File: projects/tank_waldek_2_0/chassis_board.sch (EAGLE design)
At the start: 22 parts, among them U1 NUCLEO-L432KC

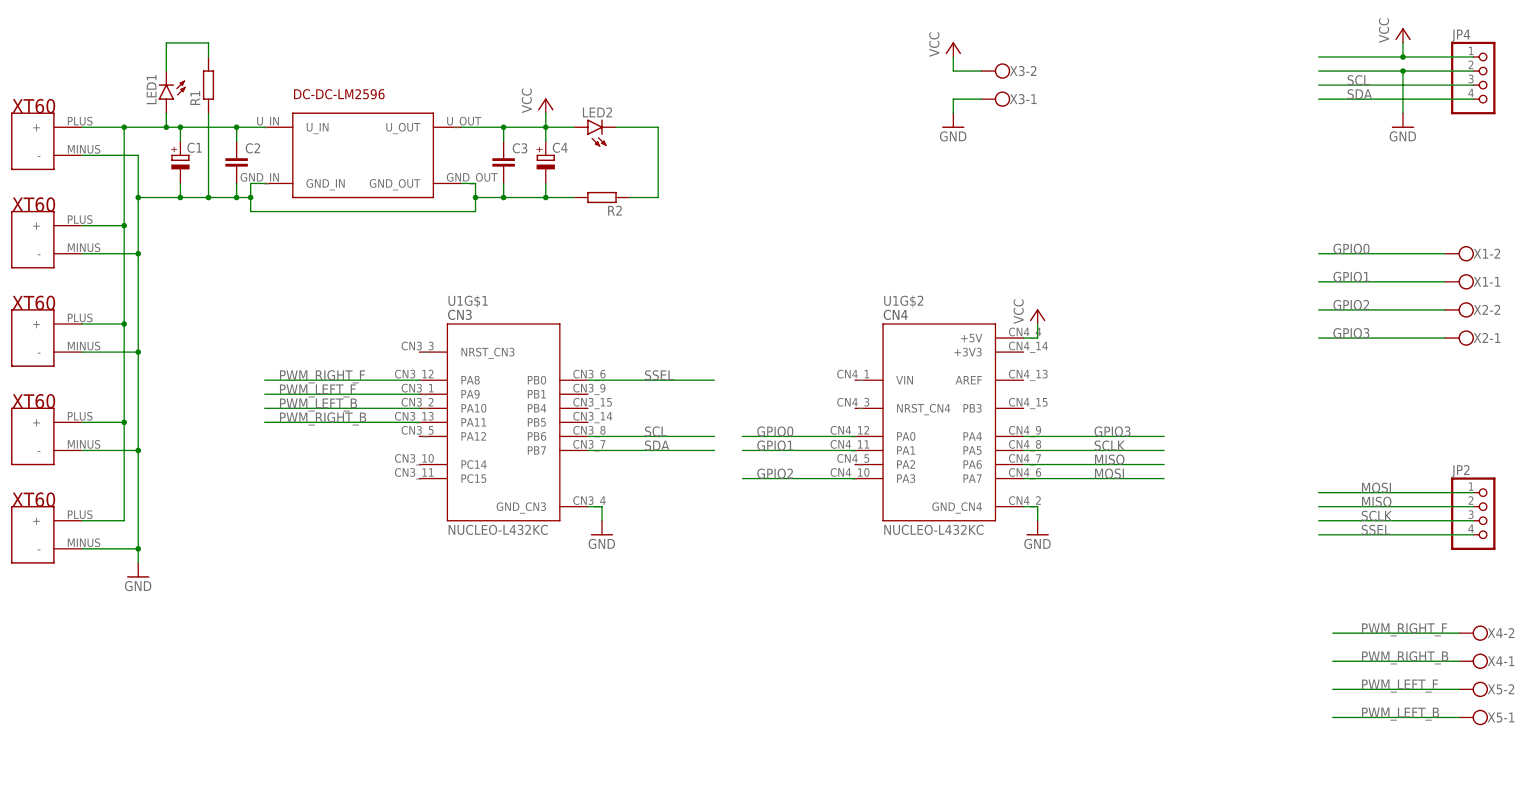
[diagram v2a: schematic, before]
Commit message: updated waldek chassis board and added new rpi shield
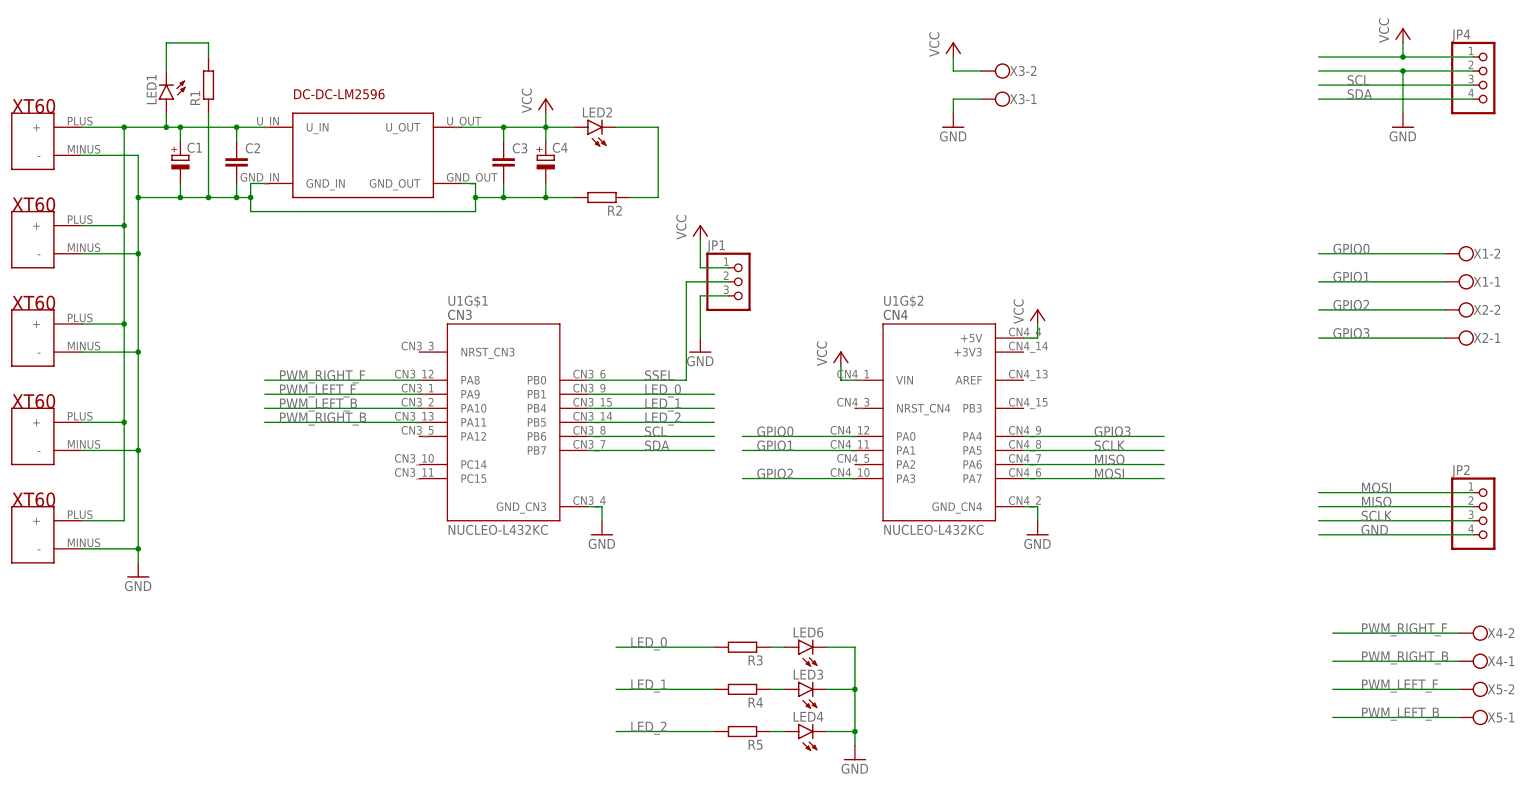
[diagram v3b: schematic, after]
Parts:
- added JP1: (no value), pinhead:PINHD-1X3
- added LED3, LED4, LED6: (no value), led:LEDSML1206
- added R3, R4, R5: (no value), rcl:R-EU_M1206
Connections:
- new net LED_0: R3.2, U1G$1.PB1
- new net LED_1: R4.2, U1G$1.PB4
- new net LED_2: R5.2, U1G$1.PB5
- new net N$3: LED6.A, R3.1
- new net N$7: LED3.A, R4.1
- new net N$8: LED4.A, R5.1
- net GND: now also JP1.3, JP2.4, LED3.C, LED4.C, LED6.C
- net SSEL: now also JP1.2; no longer JP2.4
- net VCC: now also JP1.1, U1G$2.VIN
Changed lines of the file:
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@@
 <part name="X4" library="con-wago-500" library_urn="urn:adsk.eagle:library:195" deviceset="W237-102" device="" package3d_urn="urn:adsk.eagle:package:10688/1"/>
 <part name="X5" library="con-wago-500" library_urn="urn:adsk.eagle:library:195" deviceset="W237-102" device="" package3d_urn="urn:adsk.eagle:package:10688/1"/>
+<part name="R3" library="rcl" library_urn="urn:adsk.eagle:library:334" deviceset="R-EU_" device="M1206" package3d_urn="urn:adsk.eagle:package:23566/2"/>
+<part name="R4" library="rcl" library_urn="urn:adsk.eagle:library:334" deviceset="R-EU_" device="M1206" package3d_urn="urn:adsk.eagle:package:23566/2"/>
+<part name="R5" library="rcl" library_urn="urn:adsk.eagle:library:334" deviceset="R-EU_" device="M1206" package3d_urn="urn:adsk.eagle:package:23566/2"/>
+<part name="GND6" library="supply1" library_urn="urn:adsk.eagle:library:371" deviceset="GND" device=""/>
+<part name="JP1" library="pinhead" library_urn="urn:adsk.eagle:library:325" deviceset="PINHD-1X3" device="" package3d_urn="urn:adsk.eagle:package:22458/2"/>
+<part name="P+5" library="supply1" library_urn="urn:adsk.eagle:library:371" deviceset="VCC" device=""/>
+<part name="GND7" library="supply1" library_urn="urn:adsk.eagle:library:371" deviceset="GND" device=""/>
+<part name="LED6" library="led" library_urn="urn:adsk.eagle:library:259" deviceset="LED" device="SML1206" package3d_urn="urn:adsk.eagle:package:15829/1"/>
+<part name="LED3" library="led" library_urn="urn:adsk.eagle:library:259" deviceset="LED" device="SML1206" package3d_urn="urn:adsk.eagle:package:15829/1"/>
+<part name="LED4" library="led" library_urn="urn:adsk.eagle:library:259" deviceset="LED" device="SML1206" package3d_urn="urn:adsk.eagle:package:15829/1"/>
+<part name="P+6" library="supply1" library_urn="urn:adsk.eagle:library:371" deviceset="VCC" device=""/>
 </parts>
 <sheets>
@@
 <attribute name="VALUE" x="215.9" y="-19.177" size="1.778" layer="96" rot="R180"/>
 <attribute name="NAME" x="213.36" y="-23.749" size="1.778" layer="95"/>
+</instance>
+<instance part="R3" gate="G$1" x="78.74" y="-15.24" smashed="yes" rot="R180">
+<attribute name="NAME" x="82.55" y="-16.7386" size="1.778" layer="95" rot="R180"/>
+<attribute name="VALUE" x="82.55" y="-11.938" size="1.778" layer="96" rot="R180"/>
+</instance>
+<instance part="R4" gate="G$1" x="78.74" y="-22.86" smashed="yes" rot="R180">
+<attribute name="NAME" x="82.55" y="-24.3586" size="1.778" layer="95" rot="R180"/>
+<attribute name="VALUE" x="82.55" y="-19.558" size="1.778" layer="96" rot="R180"/>
+</instance>
+<instance part="R5" gate="G$1" x="78.74" y="-30.48" smashed="yes" rot="R180">
+<attribute name="NAME" x="82.55" y="-31.9786" size="1.778" layer="95" rot="R180"/>
+<attribute name="VALUE" x="82.55" y="-27.178" size="1.778" layer="96" rot="R180"/>
+</instance>
+<instance part="GND6" gate="1" x="99.06" y="-35.56" smashed="yes">
+<attribute name="VALUE" x="96.52" y="-38.1" size="1.778" layer="96"/>
+</instance>
+<instance part="JP1" gate="A" x="78.74" y="50.8" smashed="yes">
+<attribute name="NAME" x="72.39" y="56.515" size="1.778" layer="95"/>
+<attribute name="VALUE" x="72.39" y="43.18" size="1.778" layer="96"/>
+</instance>
+<instance part="P+5" gate="VCC" x="71.12" y="60.96" smashed="yes">
+<attribute name="VALUE" x="68.58" y="58.42" size="1.778" layer="96" rot="R90"/>
+</instance>
+<instance part="GND7" gate="1" x="71.12" y="38.1" smashed="yes">
+<attribute name="VALUE" x="68.58" y="35.56" size="1.778" layer="96"/>
+</instance>
+<instance part="LED6" gate="G$1" x="88.9" y="-15.24" smashed="yes" rot="R90">
+<attribute name="NAME" x="93.472" y="-11.684" size="1.778" layer="95" rot="R180"/>
+<attribute name="VALUE" x="93.472" y="-9.525" size="1.778" layer="96" rot="R180"/>
+</instance>
+<instance part="LED3" gate="G$1" x="88.9" y="-22.86" smashed="yes" rot="R90">
+<attribute name="NAME" x="93.472" y="-19.304" size="1.778" layer="95" rot="R180"/>
+<attribute name="VALUE" x="93.472" y="-17.145" size="1.778" layer="96" rot="R180"/>
+</instance>
+<instance part="LED4" gate="G$1" x="88.9" y="-30.48" smashed="yes" rot="R90">
+<attribute name="NAME" x="93.472" y="-26.924" size="1.778" layer="95" rot="R180"/>
+<attribute name="VALUE" x="93.472" y="-24.765" size="1.778" layer="96" rot="R180"/>
+</instance>
+<instance part="P+6" gate="VCC" x="96.52" y="38.1" smashed="yes">
+<attribute name="VALUE" x="93.98" y="35.56" size="1.778" layer="96" rot="R90"/>
 </instance>
 </instances>
@@
 <wire x1="116.84" y1="83.82" x2="116.84" y2="81.28" width="0.1524" layer="91"/>
 </segment>
+<segment>
+<pinref part="GND6" gate="1" pin="GND"/>
+<wire x1="99.06" y1="-15.24" x2="99.06" y2="-22.86" width="0.1524" layer="91"/>
+<pinref part="LED6" gate="G$1" pin="C"/>
+<wire x1="99.06" y1="-22.86" x2="99.06" y2="-30.48" width="0.1524" layer="91"/>
+<wire x1="99.06" y1="-30.48" x2="99.06" y2="-33.02" width="0.1524" layer="91"/>
+<wire x1="93.98" y1="-15.24" x2="99.06" y2="-15.24" width="0.1524" layer="91"/>
+<pinref part="LED3" gate="G$1" pin="C"/>
+<wire x1="93.98" y1="-22.86" x2="99.06" y2="-22.86" width="0.1524" layer="91"/>
+<junction x="99.06" y="-22.86"/>
+<pinref part="LED4" gate="G$1" pin="C"/>
+<wire x1="93.98" y1="-30.48" x2="99.06" y2="-30.48" width="0.1524" layer="91"/>
+<junction x="99.06" y="-30.48"/>
+</segment>
+<segment>
+<pinref part="JP2" gate="A" pin="4"/>
+<wire x1="210.82" y1="5.08" x2="182.88" y2="5.08" width="0.1524" layer="91"/>
+<label x="190.5" y="5.08" size="1.778" layer="95"/>
+</segment>
+<segment>
+<pinref part="JP1" gate="A" pin="3"/>
+<wire x1="76.2" y1="48.26" x2="71.12" y2="48.26" width="0.1524" layer="91"/>
+<wire x1="71.12" y1="48.26" x2="71.12" y2="40.64" width="0.1524" layer="91"/>
+<pinref part="GND7" gate="1" pin="GND"/>
+</segment>
 </net>
 <net name="VCC" class="0">
@@
 <pinref part="P+4" gate="VCC" pin="VCC"/>
 <wire x1="116.84" y1="88.9" x2="116.84" y2="91.44" width="0.1524" layer="91"/>
+</segment>
+<segment>
+<pinref part="JP1" gate="A" pin="1"/>
+<wire x1="76.2" y1="53.34" x2="71.12" y2="53.34" width="0.1524" layer="91"/>
+<wire x1="71.12" y1="53.34" x2="71.12" y2="58.42" width="0.1524" layer="91"/>
+<pinref part="P+5" gate="VCC" pin="VCC"/>
+</segment>
+<segment>
+<pinref part="U1" gate="G$2" pin="VIN"/>
+<wire x1="99.06" y1="33.02" x2="96.52" y2="33.02" width="0.1524" layer="91"/>
+<pinref part="P+6" gate="VCC" pin="VCC"/>
+<wire x1="96.52" y1="33.02" x2="96.52" y2="35.56" width="0.1524" layer="91"/>
 </segment>
 </net>
@@
 <segment>
 <pinref part="U1" gate="G$1" pin="PB0"/>
-<wire x1="50.8" y1="33.02" x2="73.66" y2="33.02" width="0.1524" layer="91"/>
+<wire x1="50.8" y1="33.02" x2="68.58" y2="33.02" width="0.1524" layer="91"/>
 <label x="60.96" y="33.02" size="1.778" layer="95"/>
-</segment>
-<segment>
-<pinref part="JP2" gate="A" pin="4"/>
-<wire x1="210.82" y1="5.08" x2="182.88" y2="5.08" width="0.1524" layer="91"/>
-<label x="190.5" y="5.08" size="1.778" layer="95"/>
+<wire x1="68.58" y1="33.02" x2="68.58" y2="50.8" width="0.1524" layer="91"/>
+<pinref part="JP1" gate="A" pin="2"/>
+<wire x1="68.58" y1="50.8" x2="76.2" y2="50.8" width="0.1524" layer="91"/>
 </segment>
 </net>
@@
 </segment>
 </net>
+<net name="LED_0" class="0">
+<segment>
+<pinref part="U1" gate="G$1" pin="PB1"/>
+<wire x1="50.8" y1="30.48" x2="73.66" y2="30.48" width="0.1524" layer="91"/>
+<label x="60.96" y="30.48" size="1.778" layer="95"/>
+</segment>
+<segment>
+<wire x1="73.66" y1="-15.24" x2="55.88" y2="-15.24" width="0.1524" layer="91"/>
+<label x="58.42" y="-15.24" size="1.778" layer="95"/>
+<pinref part="R3" gate="G$1" pin="2"/>
+</segment>
+</net>
+<net name="LED_1" class="0">
+<segment>
+<pinref part="U1" gate="G$1" pin="PB4"/>
+<wire x1="50.8" y1="27.94" x2="73.66" y2="27.94" width="0.1524" layer="91"/>
+<label x="60.96" y="27.94" size="1.778" layer="95"/>
+</segment>
+<segment>
+<wire x1="73.66" y1="-22.86" x2="55.88" y2="-22.86" width="0.1524" layer="91"/>
+<label x="58.42" y="-22.86" size="1.778" layer="95"/>
+<pinref part="R4" gate="G$1" pin="2"/>
+</segment>
+</net>
+<net name="LED_2" class="0">
+<segment>
+<pinref part="U1" gate="G$1" pin="PB5"/>
+<wire x1="50.8" y1="25.4" x2="73.66" y2="25.4" width="0.1524" layer="91"/>
+<label x="60.96" y="25.4" size="1.778" layer="95"/>
+</segment>
+<segment>
+<wire x1="73.66" y1="-30.48" x2="55.88" y2="-30.48" width="0.1524" layer="91"/>
+<label x="58.42" y="-30.48" size="1.778" layer="95"/>
+<pinref part="R5" gate="G$1" pin="2"/>
+</segment>
+</net>
+<net name="N$3" class="0">
+<segment>
+<pinref part="R3" gate="G$1" pin="1"/>
+<pinref part="LED6" gate="G$1" pin="A"/>
+<wire x1="83.82" y1="-15.24" x2="86.36" y2="-15.24" width="0.1524" layer="91"/>
+</segment>
+</net>
+<net name="N$7" class="0">
+<segment>
+<pinref part="R4" gate="G$1" pin="1"/>
+<pinref part="LED3" gate="G$1" pin="A"/>
+<wire x1="83.82" y1="-22.86" x2="86.36" y2="-22.86" width="0.1524" layer="91"/>
+</segment>
+</net>
+<net name="N$8" class="0">
+<segment>
+<pinref part="R5" gate="G$1" pin="1"/>
+<pinref part="LED4" gate="G$1" pin="A"/>
+<wire x1="83.82" y1="-30.48" x2="86.36" y2="-30.48" width="0.1524" layer="91"/>
+</segment>
+</net>

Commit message: minor fixes of waldek 2 chassis board and rpi shield
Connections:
- net GND: no longer LED3.C, LED4.C, LED6.C
- net N$3: now also LED6.C; no longer LED6.A
- net N$7: now also LED3.C; no longer LED3.A
- net N$8: now also LED4.C; no longer LED4.A
- net VCC: now also LED3.A, LED4.A, LED6.A
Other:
- moved on the sheet: LED3, LED4, LED6
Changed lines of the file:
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@@
 <part name="R4" library="rcl" library_urn="urn:adsk.eagle:library:334" deviceset="R-EU_" device="M1206" package3d_urn="urn:adsk.eagle:package:23566/2"/>
 <part name="R5" library="rcl" library_urn="urn:adsk.eagle:library:334" deviceset="R-EU_" device="M1206" package3d_urn="urn:adsk.eagle:package:23566/2"/>
-<part name="GND6" library="supply1" library_urn="urn:adsk.eagle:library:371" deviceset="GND" device=""/>
 <part name="JP1" library="pinhead" library_urn="urn:adsk.eagle:library:325" deviceset="PINHD-1X3" device="" package3d_urn="urn:adsk.eagle:package:22458/2"/>
 <part name="P+5" library="supply1" library_urn="urn:adsk.eagle:library:371" deviceset="VCC" device=""/>
@@
 <part name="LED4" library="led" library_urn="urn:adsk.eagle:library:259" deviceset="LED" device="SML1206" package3d_urn="urn:adsk.eagle:package:15829/1"/>
 <part name="P+6" library="supply1" library_urn="urn:adsk.eagle:library:371" deviceset="VCC" device=""/>
+<part name="P+7" library="supply1" library_urn="urn:adsk.eagle:library:371" deviceset="VCC" device=""/>
 </parts>
 <sheets>
@@
 <attribute name="VALUE" x="82.55" y="-27.178" size="1.778" layer="96" rot="R180"/>
 </instance>
-<instance part="GND6" gate="1" x="99.06" y="-35.56" smashed="yes">
-<attribute name="VALUE" x="96.52" y="-38.1" size="1.778" layer="96"/>
-</instance>
 <instance part="JP1" gate="A" x="78.74" y="50.8" smashed="yes">
 <attribute name="NAME" x="72.39" y="56.515" size="1.778" layer="95"/>
@@
 <attribute name="VALUE" x="68.58" y="35.56" size="1.778" layer="96"/>
 </instance>
-<instance part="LED6" gate="G$1" x="88.9" y="-15.24" smashed="yes" rot="R90">
-<attribute name="NAME" x="93.472" y="-11.684" size="1.778" layer="95" rot="R180"/>
-<attribute name="VALUE" x="93.472" y="-9.525" size="1.778" layer="96" rot="R180"/>
-</instance>
-<instance part="LED3" gate="G$1" x="88.9" y="-22.86" smashed="yes" rot="R90">
-<attribute name="NAME" x="93.472" y="-19.304" size="1.778" layer="95" rot="R180"/>
-<attribute name="VALUE" x="93.472" y="-17.145" size="1.778" layer="96" rot="R180"/>
-</instance>
-<instance part="LED4" gate="G$1" x="88.9" y="-30.48" smashed="yes" rot="R90">
-<attribute name="NAME" x="93.472" y="-26.924" size="1.778" layer="95" rot="R180"/>
-<attribute name="VALUE" x="93.472" y="-24.765" size="1.778" layer="96" rot="R180"/>
+<instance part="LED6" gate="G$1" x="91.44" y="-15.24" smashed="yes" rot="R270">
+<attribute name="NAME" x="86.868" y="-18.796" size="1.778" layer="95"/>
+<attribute name="VALUE" x="86.868" y="-20.955" size="1.778" layer="96"/>
+</instance>
+<instance part="LED3" gate="G$1" x="91.44" y="-22.86" smashed="yes" rot="R270">
+<attribute name="NAME" x="86.868" y="-26.416" size="1.778" layer="95"/>
+<attribute name="VALUE" x="86.868" y="-28.575" size="1.778" layer="96"/>
+</instance>
+<instance part="LED4" gate="G$1" x="91.44" y="-30.48" smashed="yes" rot="R270">
+<attribute name="NAME" x="86.868" y="-34.036" size="1.778" layer="95"/>
+<attribute name="VALUE" x="86.868" y="-36.195" size="1.778" layer="96"/>
 </instance>
 <instance part="P+6" gate="VCC" x="96.52" y="38.1" smashed="yes">
 <attribute name="VALUE" x="93.98" y="35.56" size="1.778" layer="96" rot="R90"/>
+</instance>
+<instance part="P+7" gate="VCC" x="99.06" y="-7.62" smashed="yes">
+<attribute name="VALUE" x="96.52" y="-10.16" size="1.778" layer="96" rot="R90"/>
 </instance>
 </instances>
@@
 </segment>
 <segment>
-<pinref part="GND6" gate="1" pin="GND"/>
-<wire x1="99.06" y1="-15.24" x2="99.06" y2="-22.86" width="0.1524" layer="91"/>
-<pinref part="LED6" gate="G$1" pin="C"/>
-<wire x1="99.06" y1="-22.86" x2="99.06" y2="-30.48" width="0.1524" layer="91"/>
-<wire x1="99.06" y1="-30.48" x2="99.06" y2="-33.02" width="0.1524" layer="91"/>
-<wire x1="93.98" y1="-15.24" x2="99.06" y2="-15.24" width="0.1524" layer="91"/>
-<pinref part="LED3" gate="G$1" pin="C"/>
-<wire x1="93.98" y1="-22.86" x2="99.06" y2="-22.86" width="0.1524" layer="91"/>
-<junction x="99.06" y="-22.86"/>
-<pinref part="LED4" gate="G$1" pin="C"/>
-<wire x1="93.98" y1="-30.48" x2="99.06" y2="-30.48" width="0.1524" layer="91"/>
-<junction x="99.06" y="-30.48"/>
-</segment>
-<segment>
 <pinref part="JP2" gate="A" pin="4"/>
 <wire x1="210.82" y1="5.08" x2="182.88" y2="5.08" width="0.1524" layer="91"/>
@@
 <pinref part="P+6" gate="VCC" pin="VCC"/>
 <wire x1="96.52" y1="33.02" x2="96.52" y2="35.56" width="0.1524" layer="91"/>
+</segment>
+<segment>
+<wire x1="99.06" y1="-10.16" x2="99.06" y2="-15.24" width="0.1524" layer="91"/>
+<pinref part="P+7" gate="VCC" pin="VCC"/>
+<pinref part="LED4" gate="G$1" pin="A"/>
+<wire x1="99.06" y1="-15.24" x2="99.06" y2="-22.86" width="0.1524" layer="91"/>
+<wire x1="99.06" y1="-22.86" x2="99.06" y2="-30.48" width="0.1524" layer="91"/>
+<wire x1="93.98" y1="-30.48" x2="99.06" y2="-30.48" width="0.1524" layer="91"/>
+<pinref part="LED3" gate="G$1" pin="A"/>
+<wire x1="93.98" y1="-22.86" x2="99.06" y2="-22.86" width="0.1524" layer="91"/>
+<junction x="99.06" y="-22.86"/>
+<pinref part="LED6" gate="G$1" pin="A"/>
+<wire x1="93.98" y1="-15.24" x2="99.06" y2="-15.24" width="0.1524" layer="91"/>
+<junction x="99.06" y="-15.24"/>
 </segment>
 </net>
@@
 <segment>
 <pinref part="R3" gate="G$1" pin="1"/>
-<pinref part="LED6" gate="G$1" pin="A"/>
+<pinref part="LED6" gate="G$1" pin="C"/>
 <wire x1="83.82" y1="-15.24" x2="86.36" y2="-15.24" width="0.1524" layer="91"/>
 </segment>
@@
 <segment>
 <pinref part="R4" gate="G$1" pin="1"/>
-<pinref part="LED3" gate="G$1" pin="A"/>
+<pinref part="LED3" gate="G$1" pin="C"/>
 <wire x1="83.82" y1="-22.86" x2="86.36" y2="-22.86" width="0.1524" layer="91"/>
 </segment>
@@
 <segment>
 <pinref part="R5" gate="G$1" pin="1"/>
-<pinref part="LED4" gate="G$1" pin="A"/>
+<pinref part="LED4" gate="G$1" pin="C"/>
 <wire x1="83.82" y1="-30.48" x2="86.36" y2="-30.48" width="0.1524" layer="91"/>
 </segment>
